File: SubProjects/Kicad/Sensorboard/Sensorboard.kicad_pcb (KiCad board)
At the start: 2 copper layers, 60 x 44 mm, 26 parts, among them P1 ToyRaceCar_V2_REV3_J4, P2 ToyRaceCar_V2_REV3_J3, P3 ToyRaceCar_V2_REV3_J2, P4 ToyRaceCar_V2_REV3_J1, P5 MPU-6050, P6 ToyRaceCar_V2_REV3_J5, P7 CNY70, P8 SS495A, Q1 BSS138, Q2 BSS138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

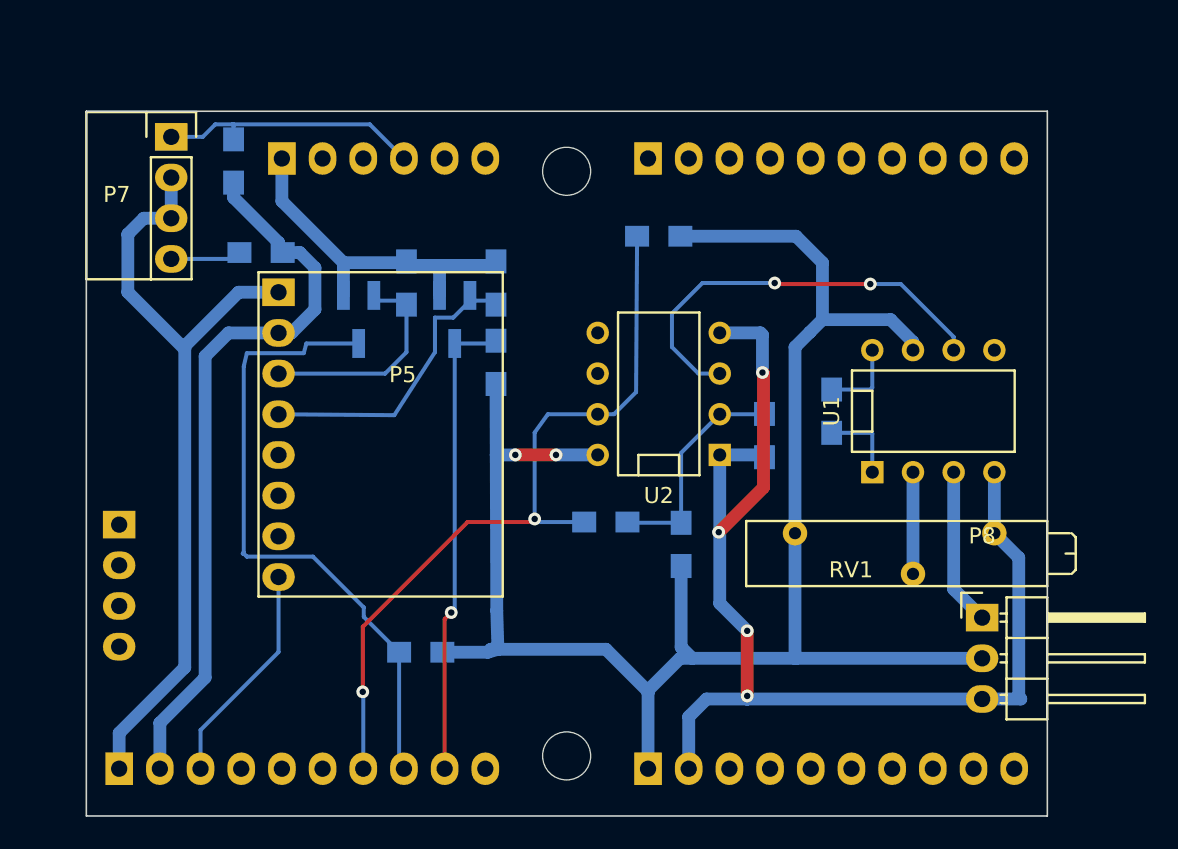
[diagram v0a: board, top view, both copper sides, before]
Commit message: Updated pcb with the brake system
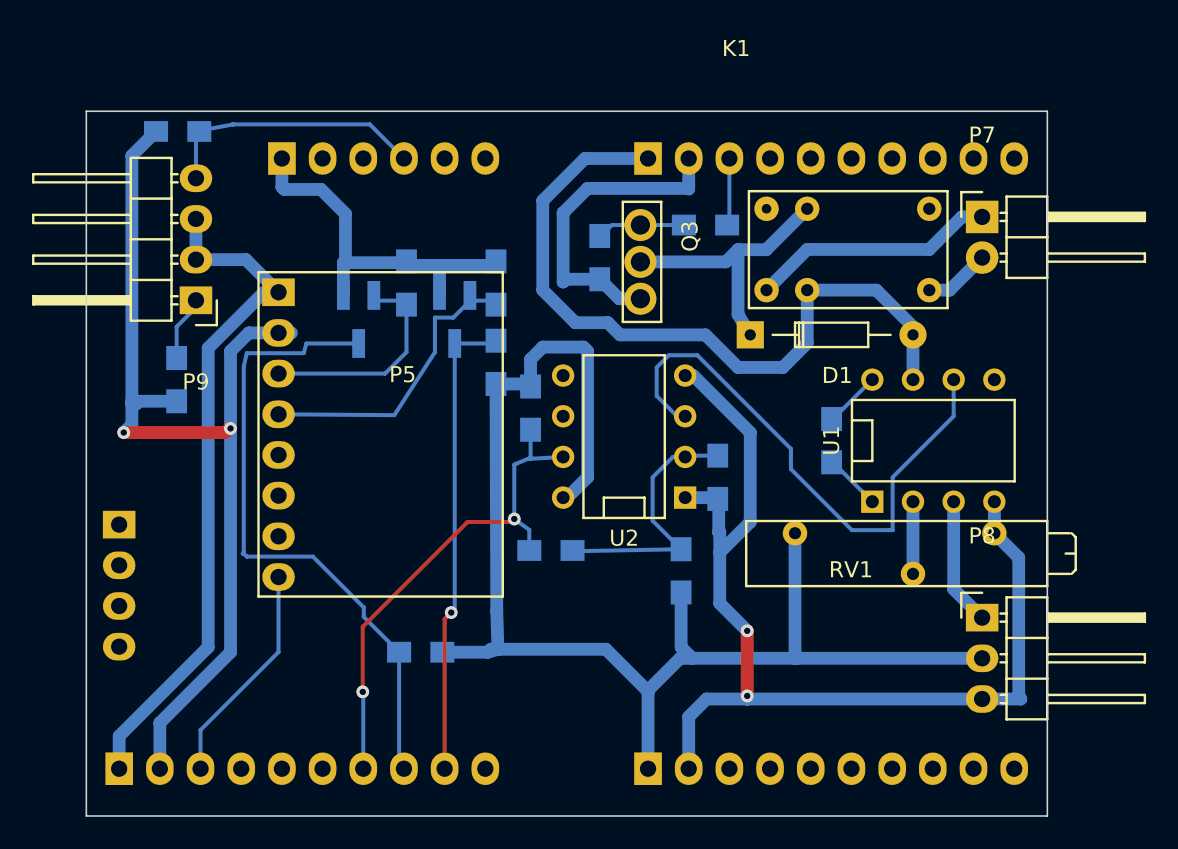
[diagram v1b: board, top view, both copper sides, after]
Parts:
- removed REF** (x2): MountingHole_3mm, Sensorboard:MountingHole_3mm-7mm
- added D1: D, Diodes_ThroughHole:Diode_DO-35_SOD27_Horizontal_RM10, F.Cu at (160.9, 98.2)
- added K1: Omron_g5v1, Sensorboard:Omron-G5V1, F.Cu at (161.9, 90.3)
- added P9: CNY70, Pin_Headers:Pin_Header_Angled_1x04, F.Cu at (126.3, 96.1)
- added Q3: Q_NMOS_GDS, Sensorboard:CASE369D, F.Cu at (154.0, 91.4)
- added R12: 100R, Resistors_SMD:R_0805_HandSoldering, B.Cu at (158.1, 91.4)
- added R13: 1M, Resistors_SMD:R_0805_HandSoldering, B.Cu at (151.5, 93.4)
- P7: value CNY70 -> CONN_01X02; footprint Sensorboard:KK254-4 -> Pin_Headers:Pin_Header_Angled_1x02
- moved P7 50.9 mm to (175.4, 90.8)
- moved R11 13.4 mm to (147.2, 102.8), turned to 270 degrees
- moved R6 9.53 mm to (125.1, 101.0), turned to 270 degrees
- moved R5 3.95 mm to (125.1, 85.5), turned to 0 degrees
- moved R7 3.91 mm to (158.9, 107.1)
- moved R8 3.86 mm to (148.4, 111.7)
- moved U2 3.43 mm to (153.0, 104.6)
- moved R10 1.84 mm to (166.0, 104.8)
- moved U1 1.84 mm to (172.3, 104.8)
- moved R9 1.65 mm to (156.6, 112.9)
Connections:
- P3 pad 3: Net-(P3-Pad3) -> /Brake
- P7 pad 1: Net-(P4-Pad4) -> Net-(K1-Pad10)
- P7 pad 2: /+5V -> Net-(K1-Pad6)
- R6 pad 1: Net-(P7-Pad4) -> Net-(P9-Pad1)
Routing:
- net /GND: track 120.9 -> 149.4 mm
- net Net-(D1-Pad1): track 0.00 -> 17.3 mm
- net /+5V: track 162.4 -> 178.8 mm, vias 2 -> 0
- net /PD6: track 48.2 -> 32.1 mm
- net Net-(K1-Pad10): track 0.00 -> 15.4 mm
- net /AD623AN_Out: track 26.4 -> 35.4 mm, vias 2 -> 0
- net Net-(Q3-Pad1): track 0.00 -> 5.54 mm
- net Net-(P7-Pad4): track 4.59 -> 0.00 mm
- net /Brake: track 0.00 -> 4.21 mm
- net Net-(K1-Pad6): track 0.00 -> 4.14 mm
- net Net-(P9-Pad1): track 0.00 -> 4.10 mm
- net Net-(R7-Pad1): track 13.9 -> 16.8 mm
- net /+3.3V: track 21.6 -> 23.9 mm
- net Net-(RV1-Pad2): track 6.35 -> 4.51 mm
- net Net-(P8-Pad1): track 9.82 -> 7.98 mm
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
